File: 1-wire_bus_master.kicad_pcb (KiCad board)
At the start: 2 copper layers, 45.7 x 40.6 mm, 6 parts

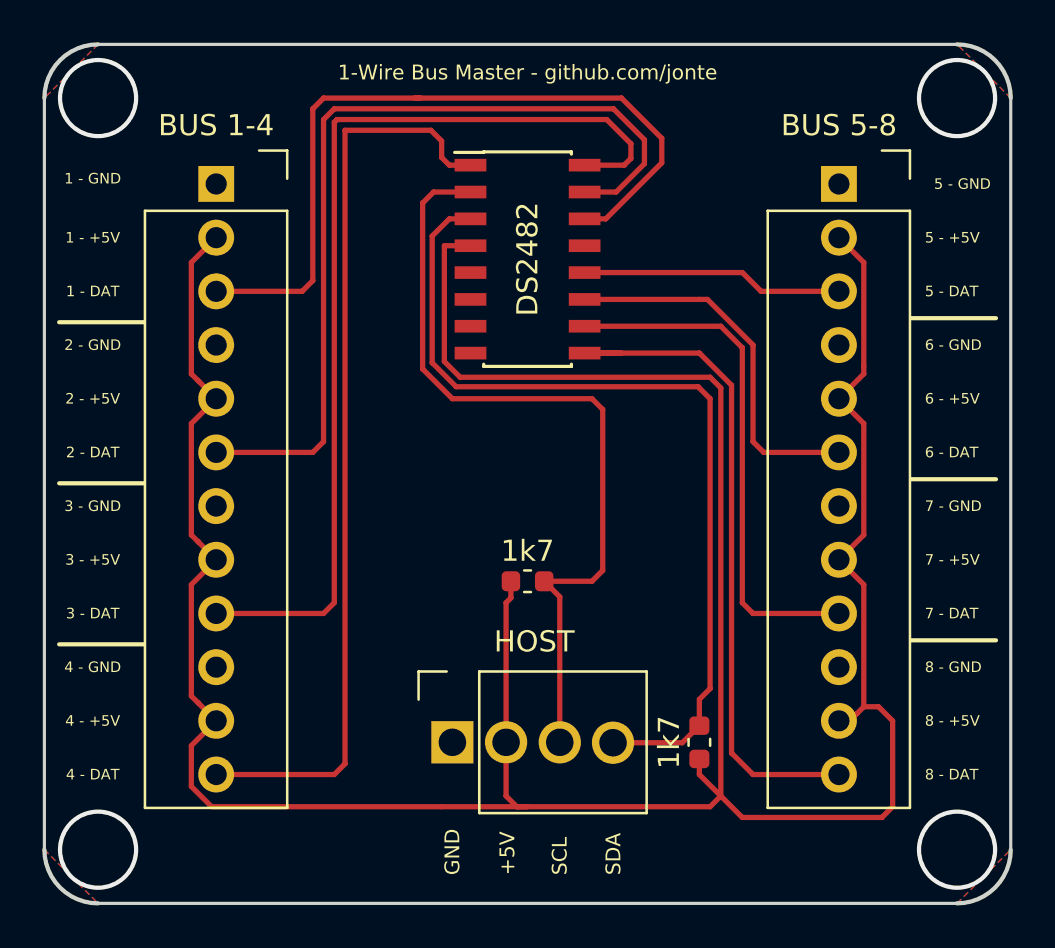
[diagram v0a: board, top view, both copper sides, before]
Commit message: Make SDA & SCL pull-ups optional, document Pi usage
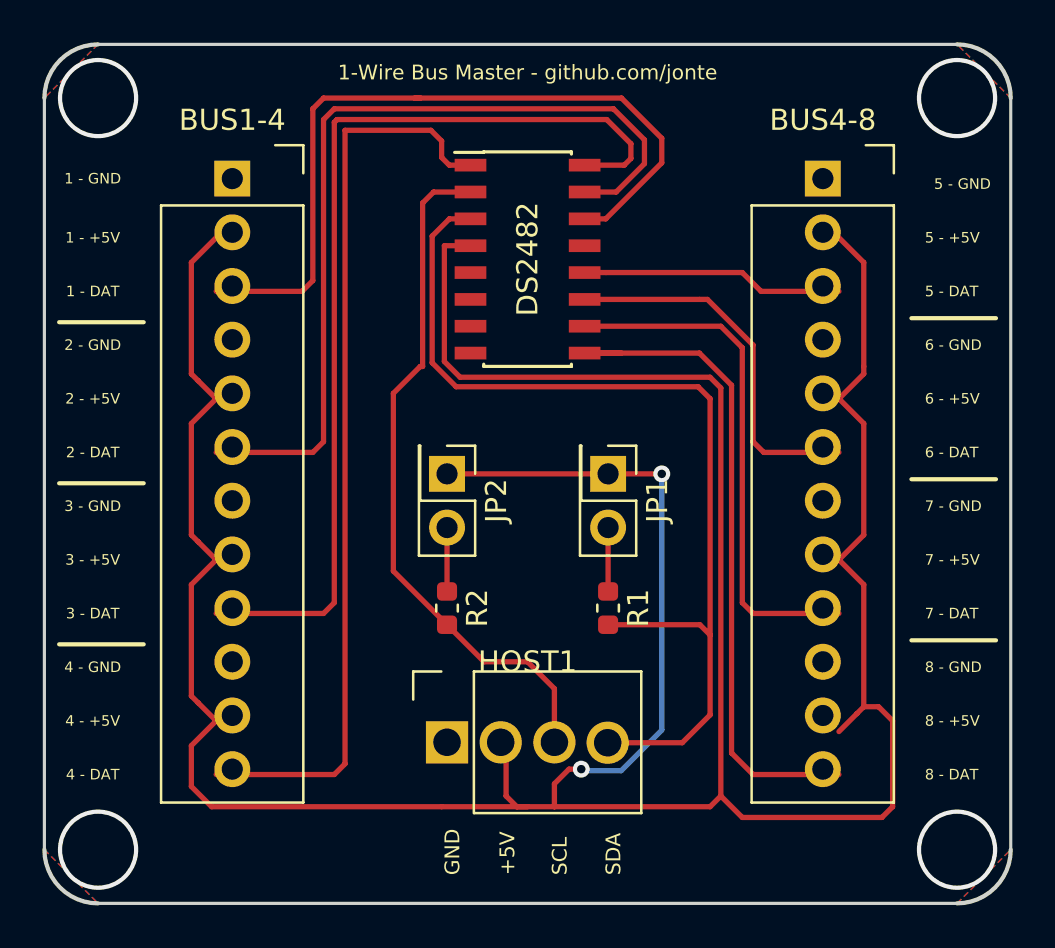
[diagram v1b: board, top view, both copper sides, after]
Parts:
- removed 1k7 (x2): 1k7, Resistor_SMD:R_0603_1608Metric
- removed BUS 1-4: Conn_01x12, 1-wire_bus_master:OSTVN12A150
- removed BUS 5-8: Conn_01x12, 1-wire_bus_master:OSTVN12A150
- removed HOST: Conn_01x04, 1-wire_bus_master:OSTVN04A150
- added BUS1-4: Conn_01x12, 1-wire_bus_master:OSTVN12A150, F.Cu at (143.5, 90.2)
- added BUS4-8: Conn_01x12, 1-wire_bus_master:OSTVN12A150, F.Cu at (171.4, 90.2)
- added HOST1: Conn_01x04, 1-wire_bus_master:OSTVN04A150, F.Cu at (153.7, 116.8)
- added JP1: JMP_PU_SDA, Connector_PinHeader_2.54mm:PinHeader_2x01_P2.54mm_Vertical, F.Cu at (161.3, 104.1)
- added JP2: JMP_PU_SCL, Connector_PinHeader_2.54mm:PinHeader_2x01_P2.54mm_Vertical, F.Cu at (153.7, 104.1)
- added R1: 1k7, Resistor_SMD:R_0603_1608Metric, F.Cu at (161.3, 110.5)
- added R2: 1k7, Resistor_SMD:R_0603_1608Metric, F.Cu at (153.7, 110.5)
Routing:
- net +5V: track 149.1 -> 168.7 mm, vias 0 -> 2
- net Net-(DS2482-Pad2): track 38.2 -> 33.0 mm
- net Net-(DS2482-Pad3): track 42.1 -> 47.1 mm
- net Net-(JP2-Pad2): track 0.00 -> 3.02 mm
- net Net-(JP1-Pad2): track 0.00 -> 3.02 mm
